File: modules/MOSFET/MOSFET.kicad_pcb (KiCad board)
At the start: 2 copper layers, 40.6 x 40.6 mm, 33 parts, among them J1 2, J10 11, J11 12, J12 13, J13 A0, J14 A1, J15 A2, J16 A3, J17 A4, J18 A5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

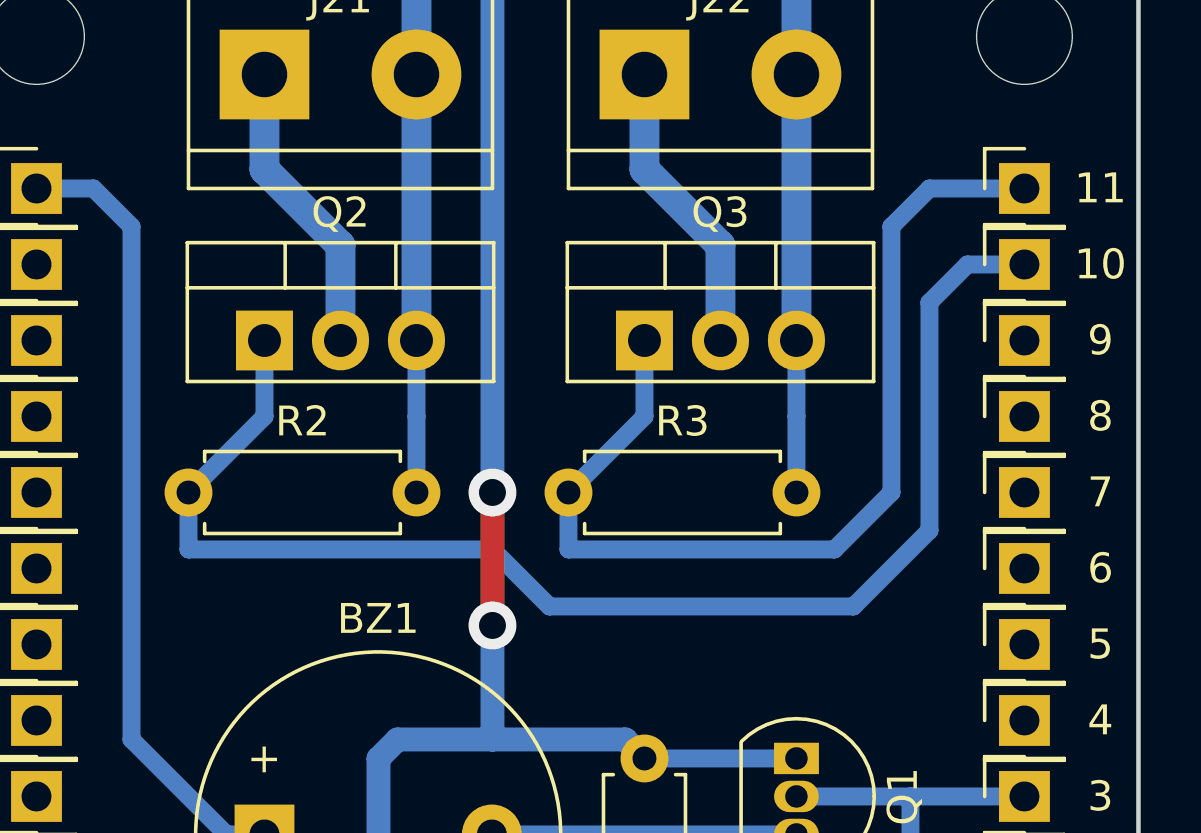
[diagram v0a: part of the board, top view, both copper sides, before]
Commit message: Fix pin numbering to v2
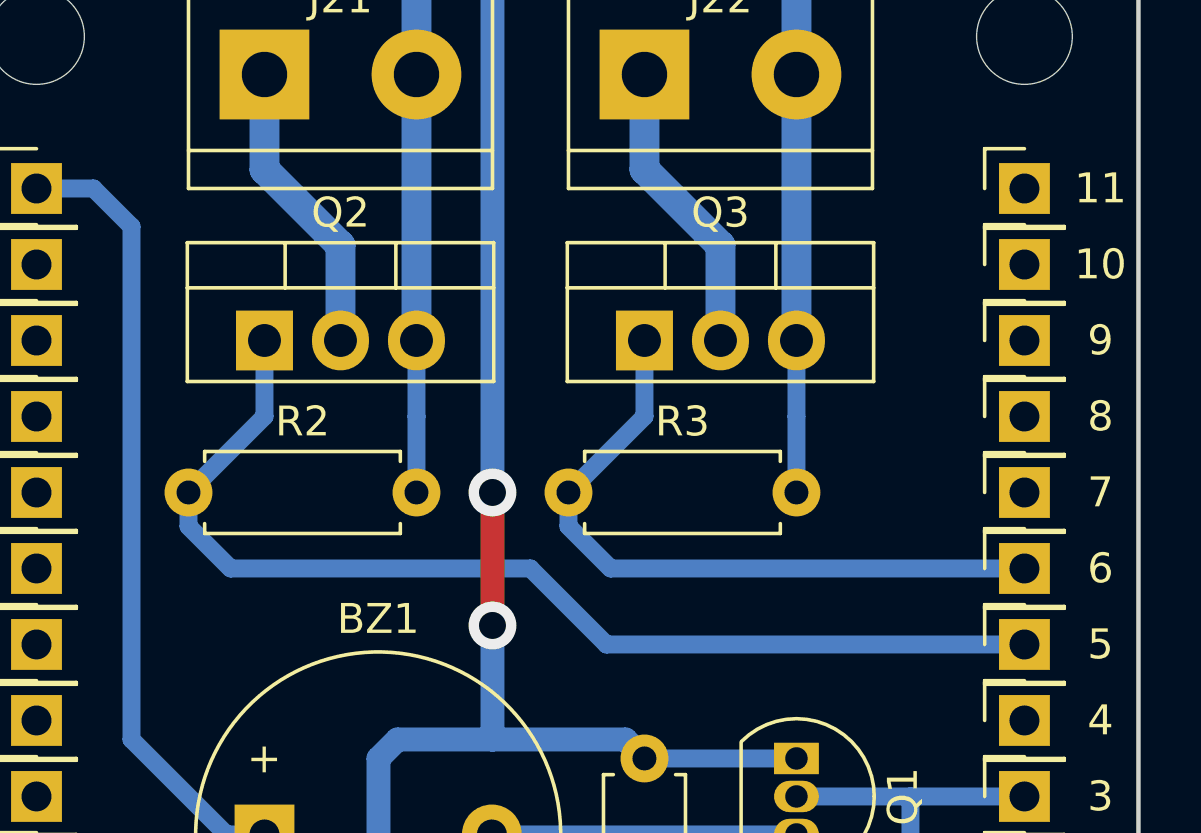
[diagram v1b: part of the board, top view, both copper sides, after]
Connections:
- Q2 pad 1: Net-(J9-Pad1) -> Net-(J4-Pad1)
- Q3 pad 1: Net-(J10-Pad1) -> Net-(J5-Pad1)
- R2 pad 1: Net-(J9-Pad1) -> Net-(J4-Pad1)
- R3 pad 1: Net-(J10-Pad1) -> Net-(J5-Pad1)
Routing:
- net Net-(J9-Pad1): track 46.0 -> 0.00 mm
- net Net-(J4-Pad1): track 0.00 -> 36.8 mm
- net Net-(J10-Pad1): track 33.5 -> 0.00 mm
- net Net-(J5-Pad1): track 0.00 -> 23.1 mm
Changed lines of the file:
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@@
     (thickness 1.6)
     (drawings 30)
-    (tracks 61)
+    (tracks 55)
     (zones 0)
     (modules 33)
@@
   )
   (setup
-    (last_trace_width 0.8)
+    (last_trace_width 0.6)
     (user_trace_width 0.6)
     (user_trace_width 0.8)
@@
       (net 22 "Net-(J21-Pad1)"))
     (pad 1 thru_hole rect (at 0 0) (size 1.905 2) (drill 1.1) (layers *.Cu *.Mask)
-      (net 9 "Net-(J9-Pad1)"))
+      (net 4 "Net-(J4-Pad1)"))
     (model ${KISYS3DMOD}/Package_TO_SOT_THT.3dshapes/TO-220-3_Vertical.wrl
       (at (xyz 0 0 0))
@@
     )
     (pad 1 thru_hole rect (at 0 0) (size 1.905 2) (drill 1.1) (layers *.Cu *.Mask)
-      (net 10 "Net-(J10-Pad1)"))
+      (net 5 "Net-(J5-Pad1)"))
     (pad 2 thru_hole oval (at 2.54 0) (size 1.905 2) (drill 1.1) (layers *.Cu *.Mask)
       (net 23 "Net-(J22-Pad1)"))
@@
     )
     (pad 1 thru_hole circle (at 0 0) (size 1.6 1.6) (drill 0.8) (layers *.Cu *.Mask)
-      (net 9 "Net-(J9-Pad1)"))
+      (net 4 "Net-(J4-Pad1)"))
     (pad 2 thru_hole oval (at 7.62 0) (size 1.6 1.6) (drill 0.8) (layers *.Cu *.Mask)
       (net 21 GND))
@@
       (net 21 GND))
     (pad 1 thru_hole circle (at 0 0) (size 1.6 1.6) (drill 0.8) (layers *.Cu *.Mask)
-      (net 10 "Net-(J10-Pad1)"))
+      (net 5 "Net-(J5-Pad1)"))
     (model ${KISYS3DMOD}/Resistor_THT.3dshapes/R_Axial_DIN0207_L6.3mm_D2.5mm_P7.62mm_Horizontal.wrl
       (at (xyz 0 0 0))
@@
   (segment (start 118.11 80.01) (end 121.92 80.01) (width 0.6) (layer B.Cu) (net 2))
   (segment (start 121.92 80.01) (end 125.73 80.01) (width 0.6) (layer B.Cu) (net 2))
-  (segment (start 113.03 67.31) (end 113.03 64.77) (width 0.6) (layer B.Cu) (net 10))
-  (segment (start 110.49 69.85) (end 113.03 67.31) (width 0.6) (layer B.Cu) (net 10))
-  (segment (start 100.33 67.31) (end 100.33 64.77) (width 0.6) (layer B.Cu) (net 9))
-  (segment (start 97.79 69.85) (end 100.33 67.31) (width 0.6) (layer B.Cu) (net 9))
-  (segment (start 123.825 62.23) (end 125.73 62.23) (width 0.6) (layer B.Cu) (net 9))
-  (segment (start 122.555 63.5) (end 123.825 62.23) (width 0.6) (layer B.Cu) (net 9))
-  (segment (start 97.79 71.755) (end 107.95 71.755) (width 0.6) (layer B.Cu) (net 9))
-  (segment (start 97.79 69.85) (end 97.79 71.755) (width 0.6) (layer B.Cu) (net 9))
-  (segment (start 107.95 71.755) (end 109.855 73.66) (width 0.6) (layer B.Cu) (net 9))
-  (segment (start 109.855 73.66) (end 120.015 73.66) (width 0.6) (layer B.Cu) (net 9))
-  (segment (start 120.015 73.66) (end 122.555 71.12) (width 0.6) (layer B.Cu) (net 9))
-  (segment (start 122.555 71.12) (end 122.555 63.5) (width 0.6) (layer B.Cu) (net 9))
-  (segment (start 122.555 59.69) (end 125.73 59.69) (width 0.6) (layer B.Cu) (net 10))
-  (segment (start 121.285 60.96) (end 122.555 59.69) (width 0.6) (layer B.Cu) (net 10))
-  (segment (start 121.285 69.85) (end 121.285 60.96) (width 0.6) (layer B.Cu) (net 10))
-  (segment (start 119.38 71.755) (end 121.285 69.85) (width 0.6) (layer B.Cu) (net 10))
-  (segment (start 110.49 69.85) (end 110.49 71.755) (width 0.6) (layer B.Cu) (net 10))
-  (segment (start 110.49 71.755) (end 119.38 71.755) (width 0.6) (layer B.Cu) (net 10))
+  (segment (start 100.33 67.31) (end 100.33 64.77) (width 0.6) (layer B.Cu) (net 4))
+  (segment (start 97.79 69.85) (end 100.33 67.31) (width 0.6) (layer B.Cu) (net 4))
+  (segment (start 97.79 70.98137) (end 99.19863 72.39) (width 0.6) (layer B.Cu) (net 4))
+  (segment (start 97.79 69.85) (end 97.79 70.98137) (width 0.6) (layer B.Cu) (net 4))
+  (segment (start 99.19863 72.39) (end 109.22 72.39) (width 0.6) (layer B.Cu) (net 4))
+  (segment (start 109.22 72.39) (end 111.76 74.93) (width 0.6) (layer B.Cu) (net 4))
+  (segment (start 111.76 74.93) (end 125.73 74.93) (width 0.6) (layer B.Cu) (net 4))
+  (segment (start 113.03 67.31) (end 113.03 64.77) (width 0.6) (layer B.Cu) (net 5))
+  (segment (start 110.49 69.85) (end 113.03 67.31) (width 0.6) (layer B.Cu) (net 5))
+  (segment (start 110.49 70.98137) (end 111.89863 72.39) (width 0.6) (layer B.Cu) (net 5))
+  (segment (start 110.49 69.85) (end 110.49 70.98137) (width 0.6) (layer B.Cu) (net 5))
+  (segment (start 111.89863 72.39) (end 125.73 72.39) (width 0.6) (layer B.Cu) (net 5))
   (segment (start 99.06 81.28) (end 100.33 81.28) (width 0.6) (layer B.Cu) (net 19))
   (segment (start 95.885 78.105) (end 99.06 81.28) (width 0.6) (layer B.Cu) (net 19))

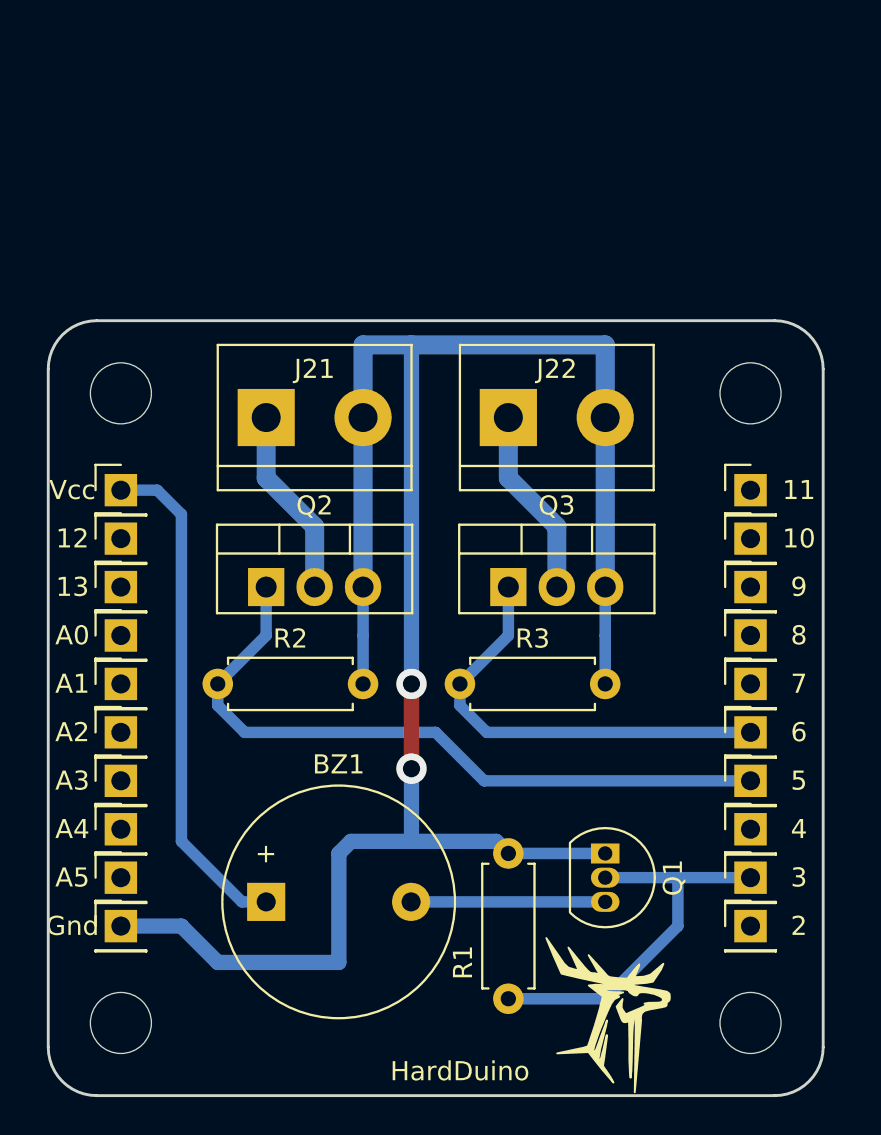
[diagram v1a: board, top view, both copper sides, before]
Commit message: MOSFET v2 pcb is ready. Change pin numbering. Add photomask.
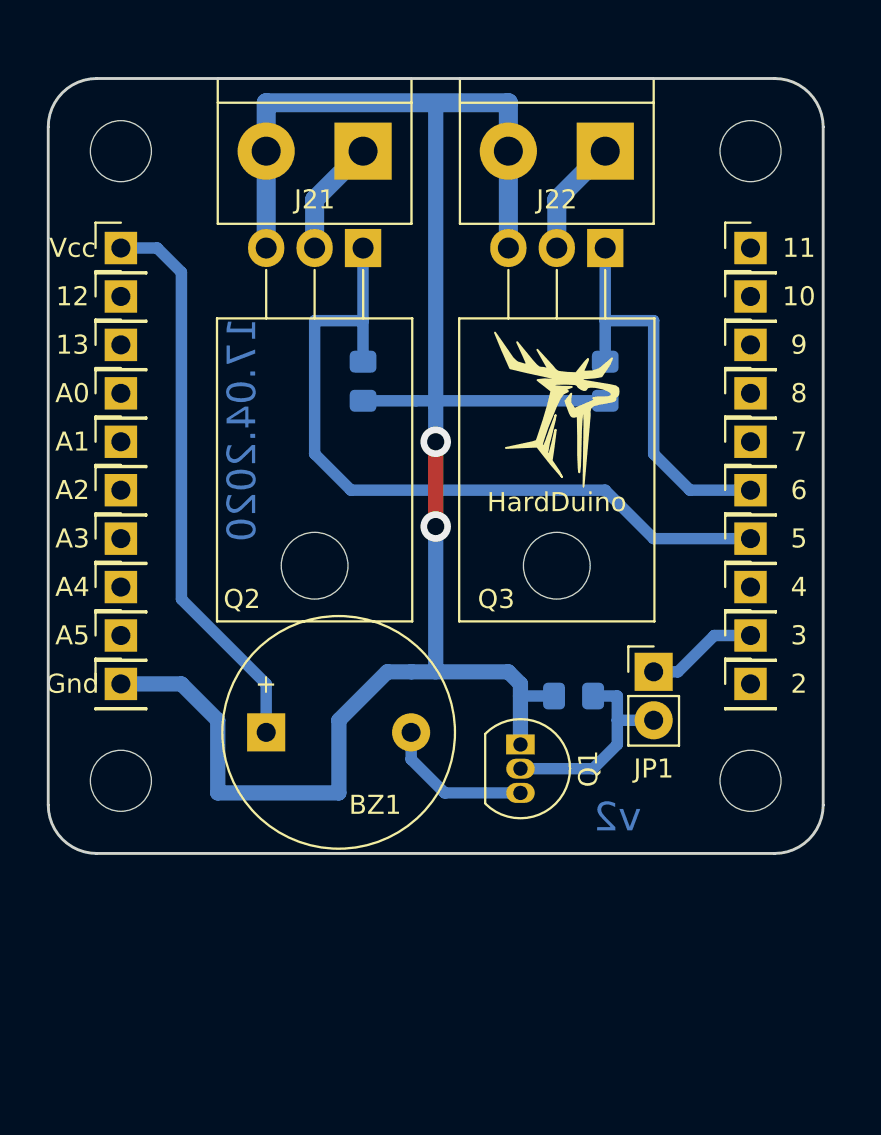
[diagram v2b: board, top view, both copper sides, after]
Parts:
- added JP1: Jumper, Connector_PinHeader_2.54mm:PinHeader_1x02_P2.54mm_Vertical, F.Cu at (120.7, 69.2)
- Q2, Q3: footprint Package_TO_SOT_THT:TO-220-3_Vertical -> Package_TO_SOT_THT:TO-220-3_Horizontal_TabDown
- R1, R2, R3: footprint Resistor_THT:R_Axial_DIN0207_L6.3mm_D2.5mm_P7.62mm_Horizontal -> Resistor_SMD:R_0805_2012Metric_Pad1.15x1.40mm_HandSolder; moved to B.Cu
- moved Q2 18.5 mm to (105.4, 47.0), turned to 180 degrees
- moved Q3 18.5 mm to (118.1, 47.0), turned to 180 degrees
- moved R3 17.6 mm to (118.1, 54.0), turned to 270 degrees
- moved R2 17.6 mm to (105.4, 54.0), turned to 270 degrees
- moved R1 16.2 mm to (116.5, 70.5), turned to 180 degrees
- moved J21 14.9 mm to (105.4, 41.9), turned to 180 degrees
- moved J22 14.9 mm to (118.1, 41.9), turned to 180 degrees
- moved J16 12.7 mm to (92.7, 62.2)
- moved J4 12.7 mm to (125.7, 62.2)
- moved H1 12.7 mm to (92.7, 41.9)
- moved H3 12.7 mm to (125.7, 41.9)
- moved J1 12.7 mm to (125.7, 69.8)
- moved J13 12.7 mm to (92.7, 54.6)
- moved J15 12.7 mm to (92.7, 59.7)
- moved J17 12.7 mm to (92.7, 64.8)
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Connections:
- Q1 pad 2: Net-(J2-Pad1) -> Net-(JP1-Pad2)
- R1 pad 1: Net-(J2-Pad1) -> Net-(JP1-Pad2)
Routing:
- net Net-(J2-Pad1): track 20.6 -> 5.87 mm
- net Net-(JP1-Pad2): track 0.00 -> 11.3 mm
- net Net-(J21-Pad1): track 9.94 -> 6.13 mm
- net Net-(J22-Pad1): track 9.94 -> 6.13 mm
- net Net-(J4-Pad1): track 36.8 -> 40.2 mm
- net VCC: track 26.6 -> 29.7 mm
- net Net-(BZ1-Pad2): track 10.2 -> 7.88 mm
- net Net-(J5-Pad1): track 23.1 -> 21.4 mm
- net GND: track 106.7 -> 105.9 mm
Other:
- board text added: "17.04.2020"
- board text added: "v2"

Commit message: Replace 2N7000 -> IRLML
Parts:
- Q1: value 2N7000 -> IRLML0030; footprint Package_TO_SOT_THT:TO-92_Inline -> Package_TO_SOT_SMD:SOT-23; moved to B.Cu
- moved R1 5.08 mm to (116.5, 75.6), turned to 270 degrees
- moved Q1 2.62 mm to (113.0, 75.6), turned to 180 degrees
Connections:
- Q1 pad 1: GND -> Net-(JP1-Pad2)
- Q1 pad 2: Net-(JP1-Pad2) -> GND
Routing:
- net GND: track 105.9 -> 110.1 mm
- net Net-(JP1-Pad2): track 11.3 -> 8.88 mm
- net Net-(BZ1-Pad2): track 7.88 -> 6.24 mm
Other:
- rule solder_mask_min_width: 0.25 -> 0.1
- board text added: "07.11.2020"
- board text added: "hash"
- board text removed: "17.04.2020"

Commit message: Add hash
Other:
- board text added: "a02f8a"
- board text removed: "hash"

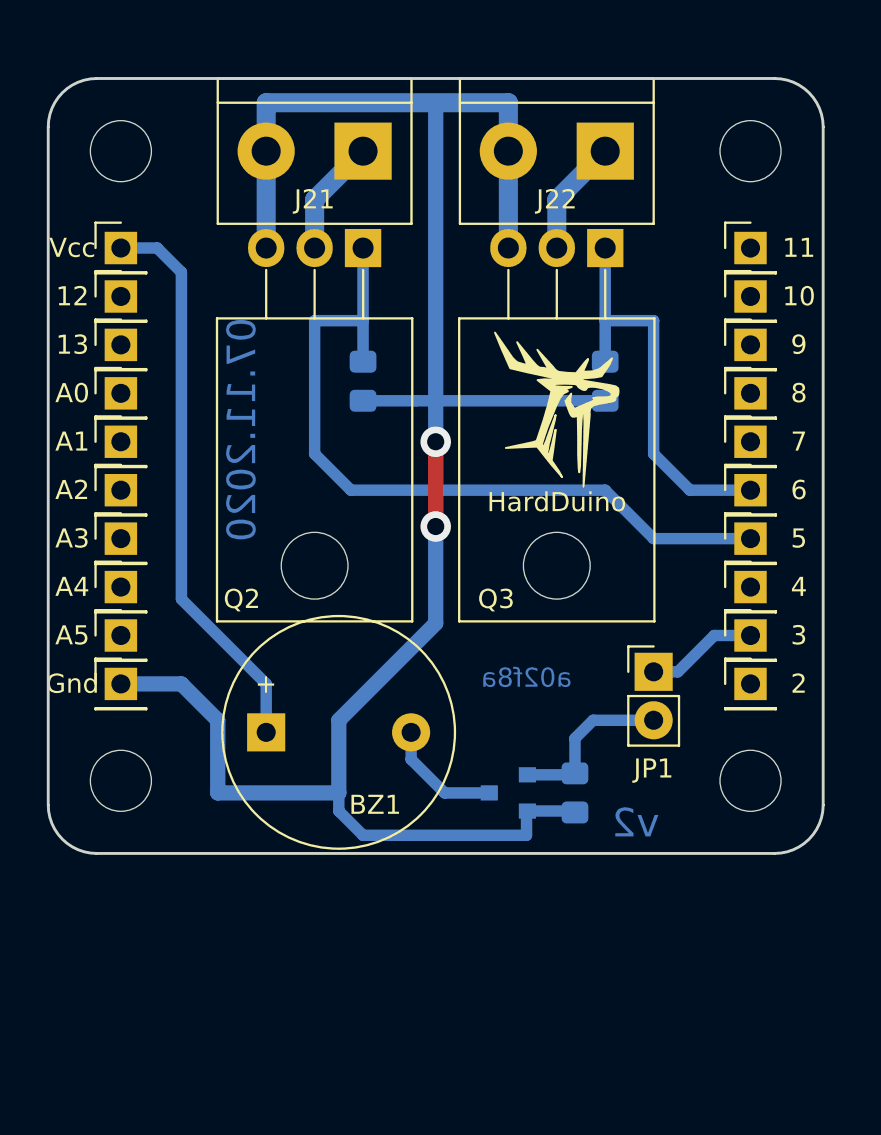
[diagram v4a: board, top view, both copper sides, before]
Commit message: 1x PCBs. Move holes to edges. Caution! This changes is uncompatible with previous versions...
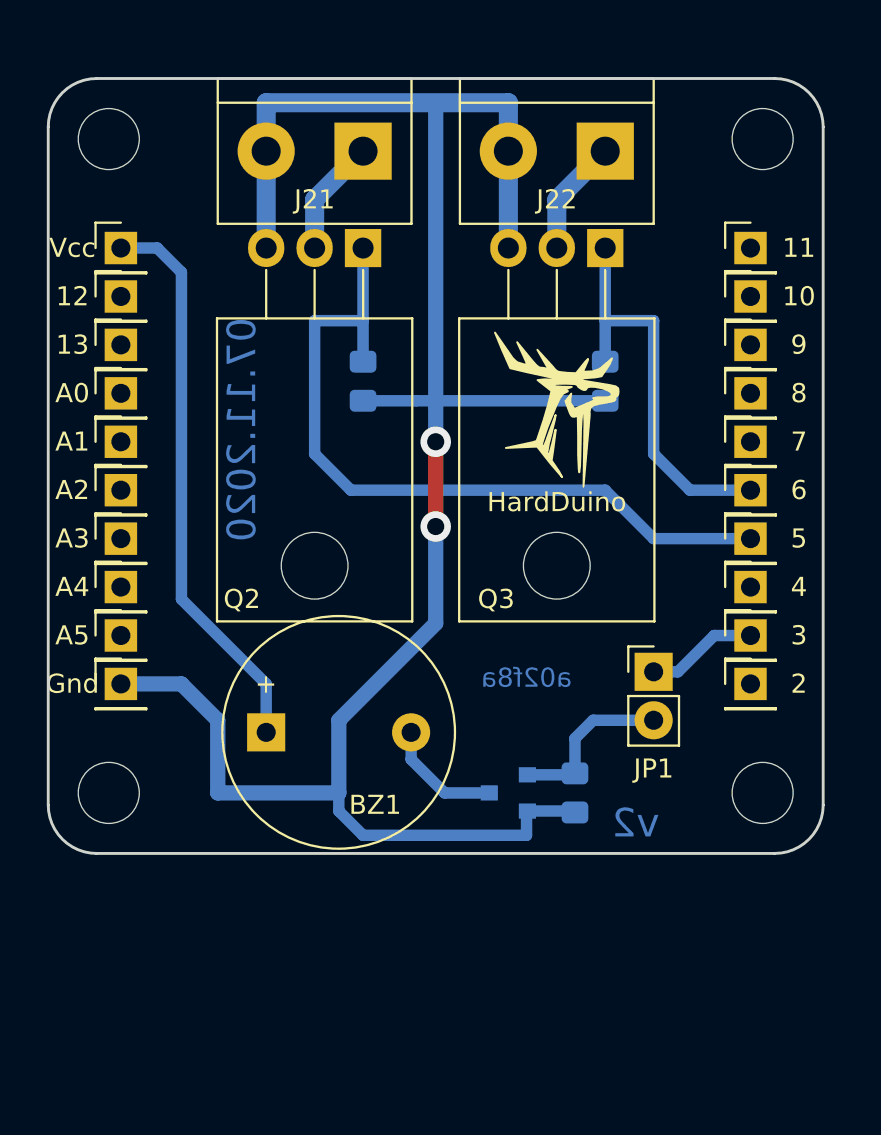
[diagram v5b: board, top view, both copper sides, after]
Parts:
- moved H1 0.90 mm to (92.1, 41.3)
- moved H3 0.90 mm to (126.4, 41.3)
- moved H2 0.90 mm to (92.1, 75.6)
- moved H4 0.90 mm to (126.4, 75.6)
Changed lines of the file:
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@@
   )
   (module MountingHole:MountingHole_3.2mm_M3 (layer F.Cu)
-    (at 92.71 41.91)
+    (at 92.0750 41.2750)
     (descr "Mounting Hole 3.2mm, no annular, M3")
     (tags "mounting hole 3.2mm no annular m3")
@@
   )
   (module MountingHole:MountingHole_3.2mm_M3 (layer F.Cu)
-    (at 92.71 74.93)
+    (at 92.0750 75.5650)
     (descr "Mounting Hole 3.2mm, no annular, M3")
     (tags "mounting hole 3.2mm no annular m3")
@@
   )
   (module MountingHole:MountingHole_3.2mm_M3 (layer F.Cu)
-    (at 125.73 41.91)
+    (at 126.3650 41.2750)
     (descr "Mounting Hole 3.2mm, no annular, M3")
     (tags "mounting hole 3.2mm no annular m3")
@@
   )
   (module MountingHole:MountingHole_3.2mm_M3 (layer F.Cu)
-    (at 125.73 74.93)
+    (at 126.3650 75.5650)
     (descr "Mounting Hole 3.2mm, no annular, M3")
     (tags "mounting hole 3.2mm no annular m3")

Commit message: Fix hash & version
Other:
- board text added: "21.02.2021"
- board text added: "b4d799"
- board text added: "v2.3"
- board text removed: "07.11.2020"
- board text removed: "a02f8a"
- board text removed: "v2"
